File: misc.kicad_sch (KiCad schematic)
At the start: 70 parts, among them U58 74F32

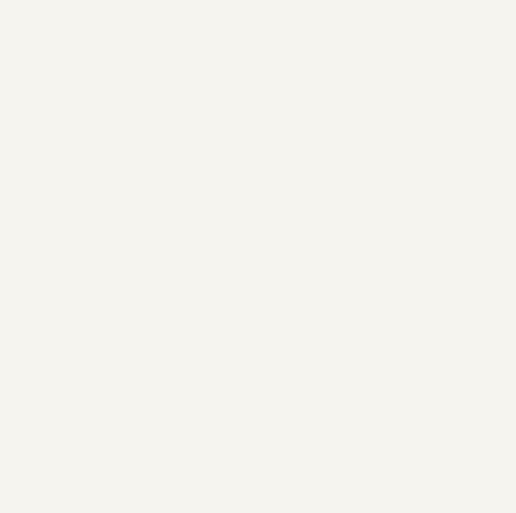
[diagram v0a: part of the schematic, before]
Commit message: add standoffs to schematic so they show up in BOM
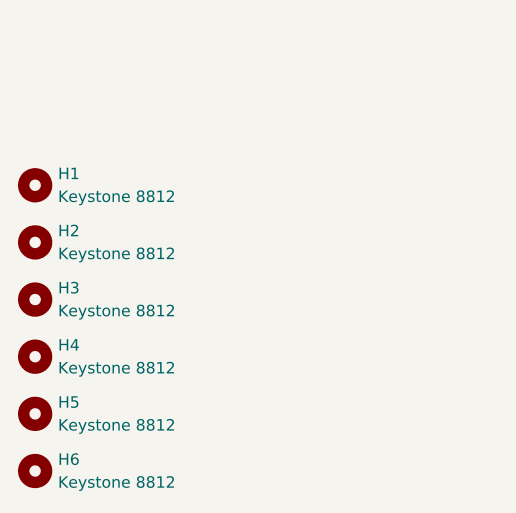
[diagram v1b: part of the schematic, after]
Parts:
- added H1, H2, H3, H4, H5, H6: Keystone 8812, MountingHole:MountingHole_4mm, symbol Mechanical:MountingHole
